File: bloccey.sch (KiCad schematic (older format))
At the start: 79 parts, among them SW1 SW_Push, SW10 SW_Push, SW11 SW_Push, SW12 SW_Push, SW13 SW_Push, SW14 SW_Push, SW15 SW_Push, SW16 SW_Push, SW17 SW_Push, SW18 SW_Push, SW19 SW_Push, SW2 SW_Push, SW20 SW_Push, SW21 SW_Push, SW22 SW_Push, SW23 SW_Push, SW24 SW_Push, SW25 SW_Push, SW26 SW_Push, SW27 SW_Push, SW28 SW_Push, SW29 SW_Push, SW3 SW_Push, SW30 SW_Push, SW31 SW_Push, SW32 SW_Push, SW33 SW_Push, SW34 SW_Push, SW35 SW_Push, SW36 SW_Push, SW37 SW_Push, SW38 SW_Push, SW39 SW_Push, SW4 SW_Push, SW40 SW_Push, SW41 SW_Push, SW42 SW_Push, SW43 SW_Push, SW44 SW_Push, SW45 SW_Push, SW46 SW_Push, SW47 SW_Push, SW48 SW_Push, SW49 SW_Push, SW5 SW_Push, SW50 SW_Push, SW51 SW_Push, SW52 SW_Push, SW53 SW_Push, SW54 SW_Push, SW55 SW_Push, SW56 SW_Push, SW57 SW_Push, SW58 SW_Push, SW59 SW_Push, SW6 SW_Push, SW60 SW_Push, SW61 SW_Push, SW62 SW_Push, SW63 SW_Push, SW64 SW_Push, SW7 SW_Push, SW8 SW_Push, SW9 SW_Push, U1 ATmega32U4-AU, Y1 16MHz

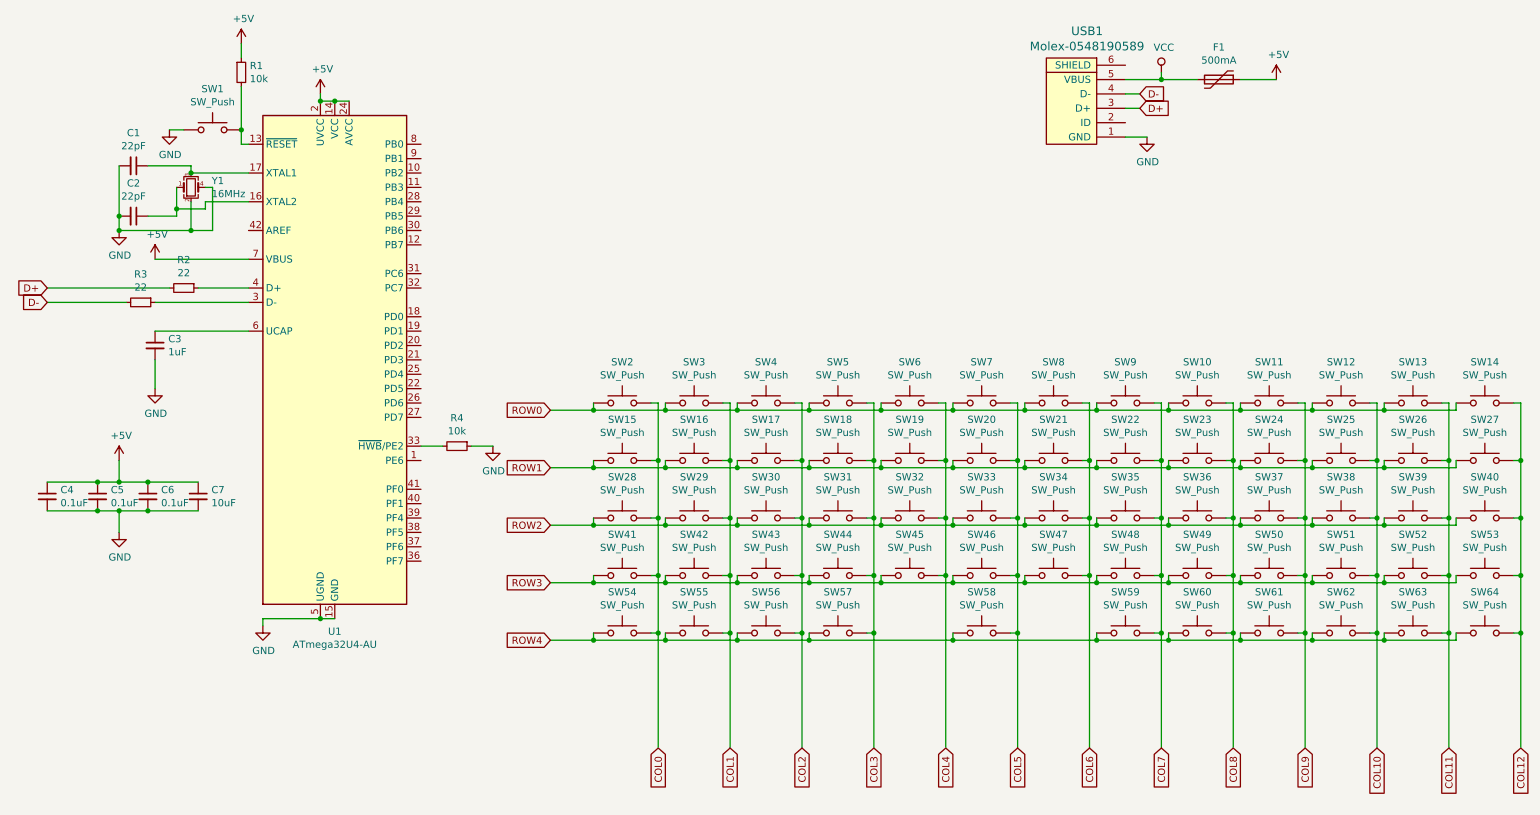
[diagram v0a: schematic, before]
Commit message: Switch to STM32, redo PCB
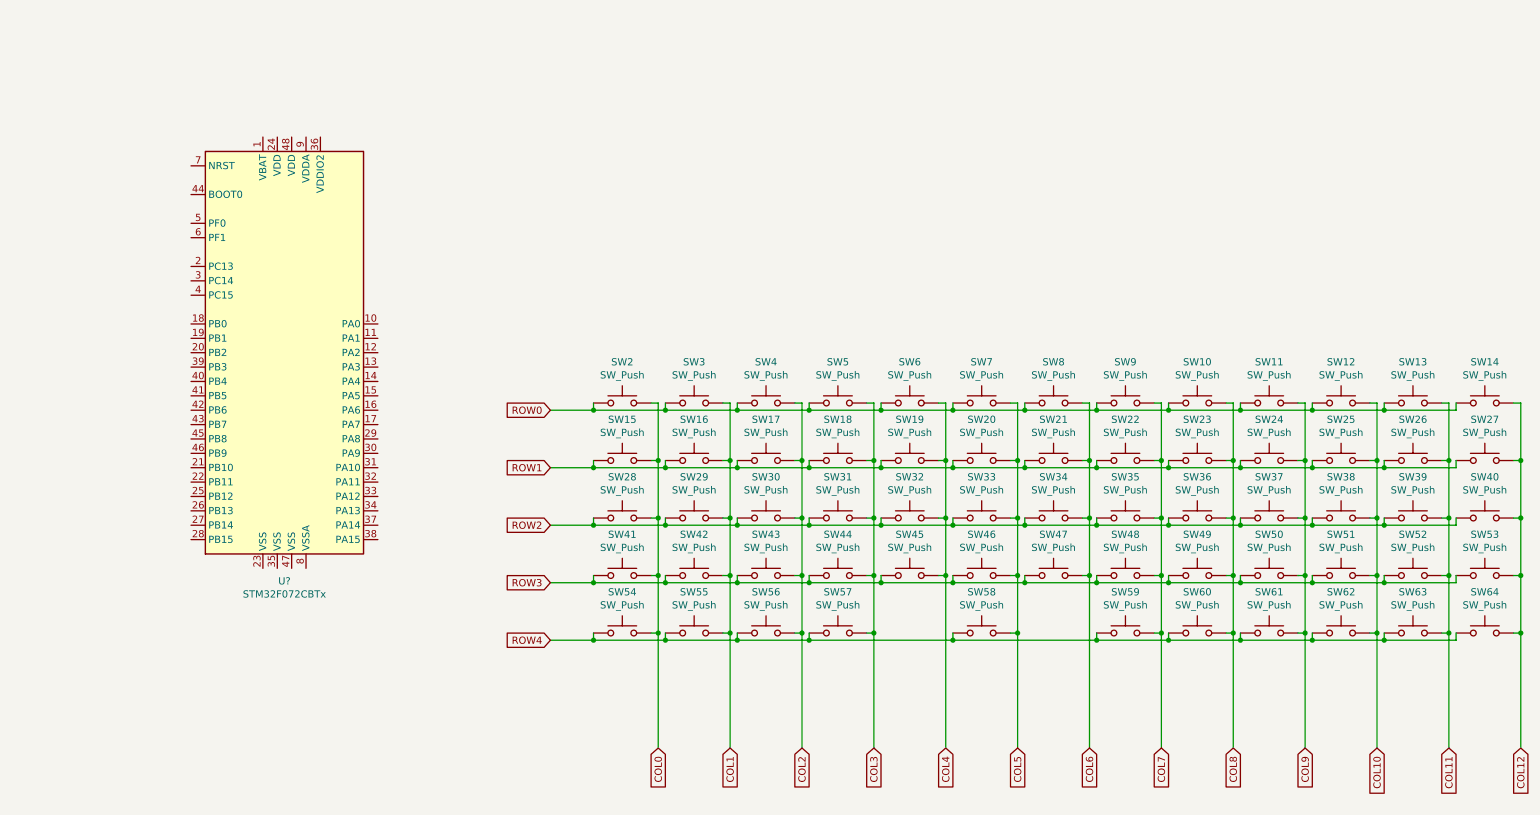
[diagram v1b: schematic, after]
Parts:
- removed C1, C2: 22pF, Capacitors_SMD:C_0805, symbol Device:C_Small
- removed C3: 1uF, Capacitors_SMD:C_0805, symbol Device:C_Small
- removed C4, C5, C6: 0.1uF, Capacitors_SMD:C_0805, symbol Device:C_Small
- removed C7: 10uF, Capacitors_SMD:C_0805, symbol Device:C_Small
- removed F1: 500mA, Fuse_Holders_and_Fuses:Fuse_SMD1206_Reflow, symbol Device:Polyfuse
- removed R1, R4: 10k, random-keyboard-parts:D_SOD-123-Pretty, symbol Device:R_Small
- removed R2, R3: 22, random-keyboard-parts:D_SOD-123-Pretty, symbol Device:R_Small
- removed SW1: SW_Push, random-keyboard-parts:PushButton_6x6mm_TH_Pretty, symbol Switch:SW_Push
- removed U1: ATmega32U4-AU, Housings_QFP:TQFP-44_10x10mm_Pitch0.8mm, symbol MCU_Microchip_ATmega:ATmega32U4-AU
- removed USB1: Molex-0548190589, random-keyboard-parts:Molex-0548190589, symbol random-keyboard-parts:Molex-0548190589
- removed Y1: 16MHz, Crystals:Crystal_SMD_3225-4pin_3.2x2.5mm, symbol Device:Crystal_GND23_Small
- added U?: STM32F072CBTx, Package_QFP:LQFP-48_7x7mm_P0.5mm, symbol MCU_ST_STM32F0:STM32F072CBTx
